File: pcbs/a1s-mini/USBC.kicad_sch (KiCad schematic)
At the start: 9 parts, among them J5 USB4105-GF-A

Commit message: Corrections and PCB layout
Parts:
- C8: value 10uF -> 10uF 10V; footprint Capacitor_SMD:C_0805_2012Metric -> Capacitor_SMD:C_0603_1608Metric; Manufacturer_Name KEMET -> Samsung Electro-Mechanics; Manufacturer_Part_Number C0805C106K8PACTU -> CL10A106KP8NNNC
- D10: footprint SamacSys_Parts:SOD3716X145N -> Diode_SMD:D_SOD-123
- D7, D8, D9: value LESD5D5.0CT1G -> TVS 5.6V; footprint SamacSys_Parts:LESD5D50CT1G -> CPDUC5V0RHF; symbol SamacSys_Parts:LESD5D5.0CT1G -> SamacSys_Parts:CPDUC5V0R-HF; Arrow Part Number (none) -> CPDUC5V0R-HF; Arrow Price/Stock (none) -> https://www.arrow.com/en/products/cpduc5v0r-hf/comchip-tech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; Height 0.7 -> 0.55; Manufacturer_Name LRC -> Comchip Technology; Manufacturer_Part_Number LESD5D5.0CT1G -> CPDUC5V0R-HF; Mouser Part Number (none) -> 750-CPDUC5V0R-HF; Mouser Price/Stock (none) -> https://www.mouser.co.uk/ProductDetail/Comchip-Technology/C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
- R20, R22: footprint Resistor_SMD:R_0805_2012Metric -> Resistor_SMD:R_0603_1608Metric; Manufacturer_Part_Number RC0805FR-075K1L -> RC0603FR-075K1L
- R4: footprint Resistor_SMD:R_0805_2012Metric -> Resistor_SMD:R_0603_1608Metric; Manufacturer_Name YAGEO -> StackPole Electronics; Manufacturer_Part_Number RC0805JR-070RL -> RMCF0603ZT0R00
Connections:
- net GND: now also J5.A1_B12 (GND), J5.B1_A12 (GND__1), R4.2

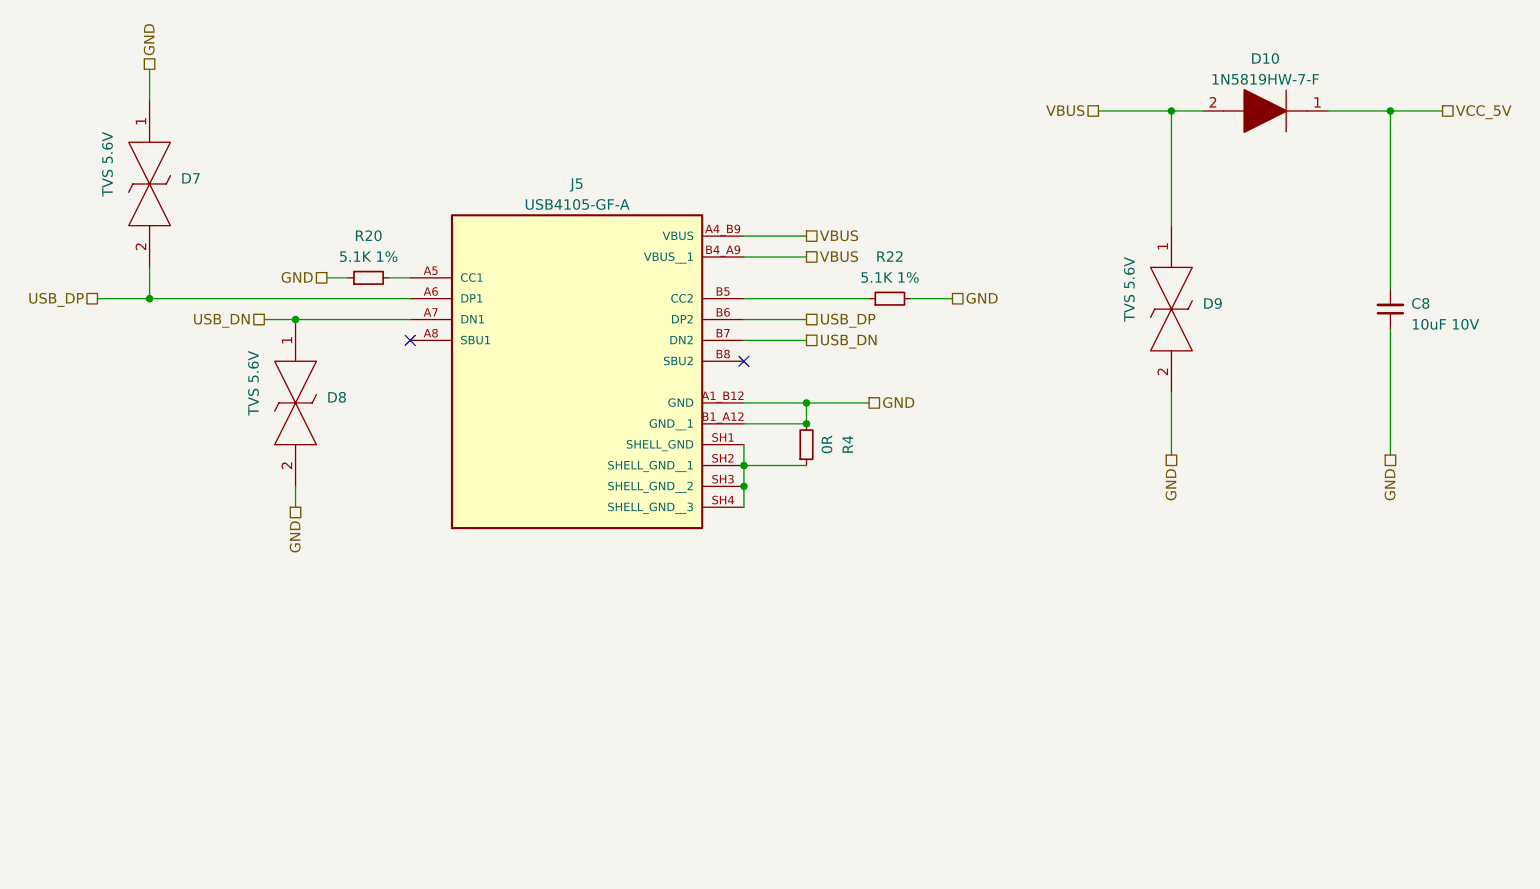
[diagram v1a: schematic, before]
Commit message: Restart A1S mini
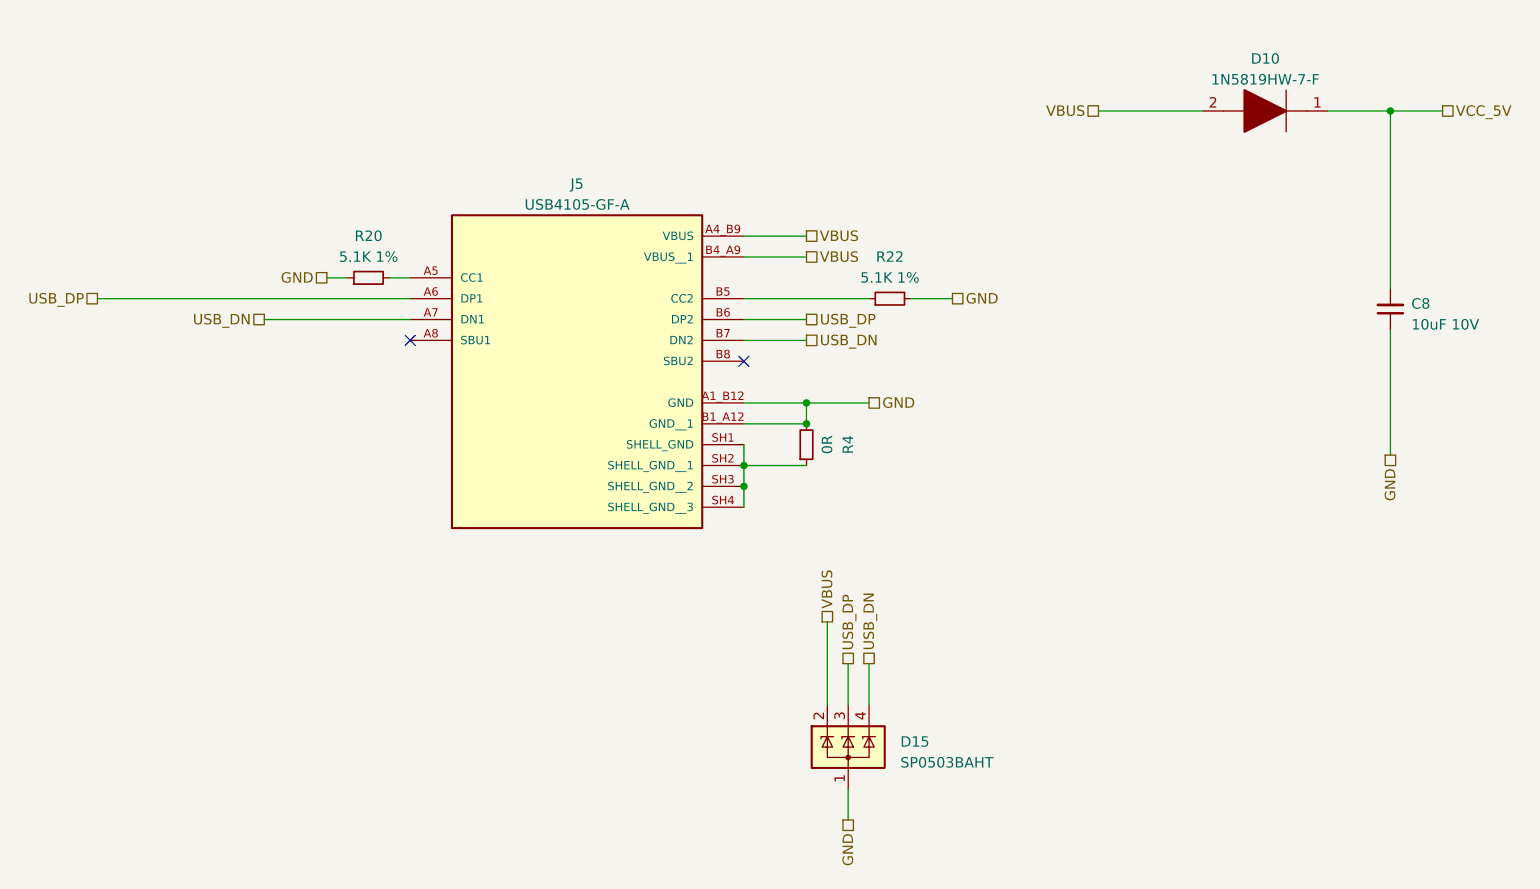
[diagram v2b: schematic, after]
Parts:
- removed D7, D8, D9: TVS 5.6V, CPDUC5V0RHF, symbol SamacSys_Parts:CPDUC5V0R-HF
- added D15: SP0503BAHT, Package_TO_SOT_SMD:SOT-143, symbol Power_Protection:SP0503BAHT
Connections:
- net GND: now also D15.1 (A)
- net USB_DN: now also D15.4 (K)
- net USB_DP: now also D15.3 (K)
- net VBUS: now also D15.2 (K)

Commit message: A1S Mini quote PCBWay
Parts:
- C8, D10, J5, R20, R22, R4: Type (none) -> SMD
- D15: value SP0503BAHT -> SP0503BAHTG; Manufacturer_Name (none) -> Littelfuse Inc; Manufacturer_Part_Number (none) -> SP0503BAHTG; Type (none) -> SMD
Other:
- company: (none) -> Martin Roger
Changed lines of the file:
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@@
 (kicad_sch (version 20230121) (generator eeschema)
   (paper "A4")
+  (title_block
+    (date "2025-03-01")
+    (rev "0.2.0")
+    (company "Martin Roger")
+  )
   (junction (at 105.41 78.74) (diameter 0) (color 0 0 0 0)
   )
@@
     )
     (property "Manufacturer_Part_Number" "USB4105-GF-A" (at 85.09 58.42 0)
+      (effects (font (size 1.27 1.27)) hide)
+    )
+    (property "Instructions/Notes" "" (at 85.09 58.42 0)
+      (effects (font (size 1.27 1.27)) hide)
+    )
+    (property "Type" "SMD" (at 85.09 58.42 0)
       (effects (font (size 1.27 1.27)) hide)
     )
@@
       (effects (font (size 1.27 1.27)) hide)
     )
+    (property "Instructions/Notes" "" (at 123.19 55.88 0)
+      (effects (font (size 1.27 1.27)) hide)
+    )
+    (property "Type" "SMD" (at 123.19 55.88 0)
+      (effects (font (size 1.27 1.27)) hide)
+    )
     (pin "1")
     (pin "2")
@@
       (effects (font (size 1.27 1.27)) hide)
     )
+    (property "Instructions/Notes" "" (at 113.03 73.66 0)
+      (effects (font (size 1.27 1.27)) hide)
+    )
+    (property "Type" "SMD" (at 113.03 73.66 0)
+      (effects (font (size 1.27 1.27)) hide)
+    )
     (pin "1")
     (pin "2")
@@
       (effects (font (size 1.27 1.27)) (justify left) hide)
     )
+    (property "Instructions/Notes" "" (at 176.53 33.02 0)
+      (effects (font (size 1.27 1.27)) hide)
+    )
+    (property "Type" "SMD" (at 176.53 33.02 0)
+      (effects (font (size 1.27 1.27)) hide)
+    )
     (pin "1")
     (pin "2")
@@
       (effects (font (size 1.27 1.27)) hide)
     )
+    (property "Instructions/Notes" "" (at 59.69 53.34 0)
+      (effects (font (size 1.27 1.27)) hide)
+    )
+    (property "Type" "SMD" (at 59.69 53.34 0)
+      (effects (font (size 1.27 1.27)) hide)
+    )
     (pin "1")
     (pin "2")
@@
       (effects (font (size 1.27 1.27)) hide)
     )
+    (property "Instructions/Notes" "" (at 184.15 57.15 0)
+      (effects (font (size 1.27 1.27)) hide)
+    )
+    (property "Type" "SMD" (at 184.15 57.15 0)
+      (effects (font (size 1.27 1.27)) hide)
+    )
     (pin "1")
     (pin "2")
@@
       (effects (font (size 1.27 1.27)) (justify left))
     )
-    (property "Value" "SP0503BAHT" (at 124.46 112.395 0)
+    (property "Value" "SP0503BAHTG" (at 124.46 112.395 0)
       (effects (font (size 1.27 1.27)) (justify left))
     )
@@
       (effects (font (size 1.27 1.27)) hide)
     )
+    (property "Description" "TVS DIODE 5.5VWM 8.5VC SOT1434" (at 118.11 110.49 0)
+      (effects (font (size 1.27 1.27)) hide)
+    )
+    (property "Manufacturer_Name" "Littelfuse Inc" (at 118.11 110.49 0)
+      (effects (font (size 1.27 1.27)) hide)
+    )
+    (property "Manufacturer_Part_Number" "SP0503BAHTG" (at 118.11 110.49 0)
+      (effects (font (size 1.27 1.27)) hide)
+    )
+    (property "Instructions/Notes" "" (at 118.11 110.49 0)
+      (effects (font (size 1.27 1.27)) hide)
+    )
+    (property "Type" "SMD" (at 118.11 110.49 0)
+      (effects (font (size 1.27 1.27)) hide)
+    )

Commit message: Projects consistency update
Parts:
- D10: footprint Diode_SMD:D_SOD-123 -> DIY:SOD3716X145N; symbol SamacSys_Parts:1N5819HW-7-F -> DIY:1N5819HW-7-F
- J5: symbol USB4105-GF-A:USB4105-GF-A -> DIY:USB4105-GF-A
- renumbered C8 to C12, D15 to D7, R4 to R21
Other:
- title: (none) -> A1S Mini Board
